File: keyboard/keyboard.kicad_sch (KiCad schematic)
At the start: 19 parts, among them U1 Raspberry_Pi_Pico

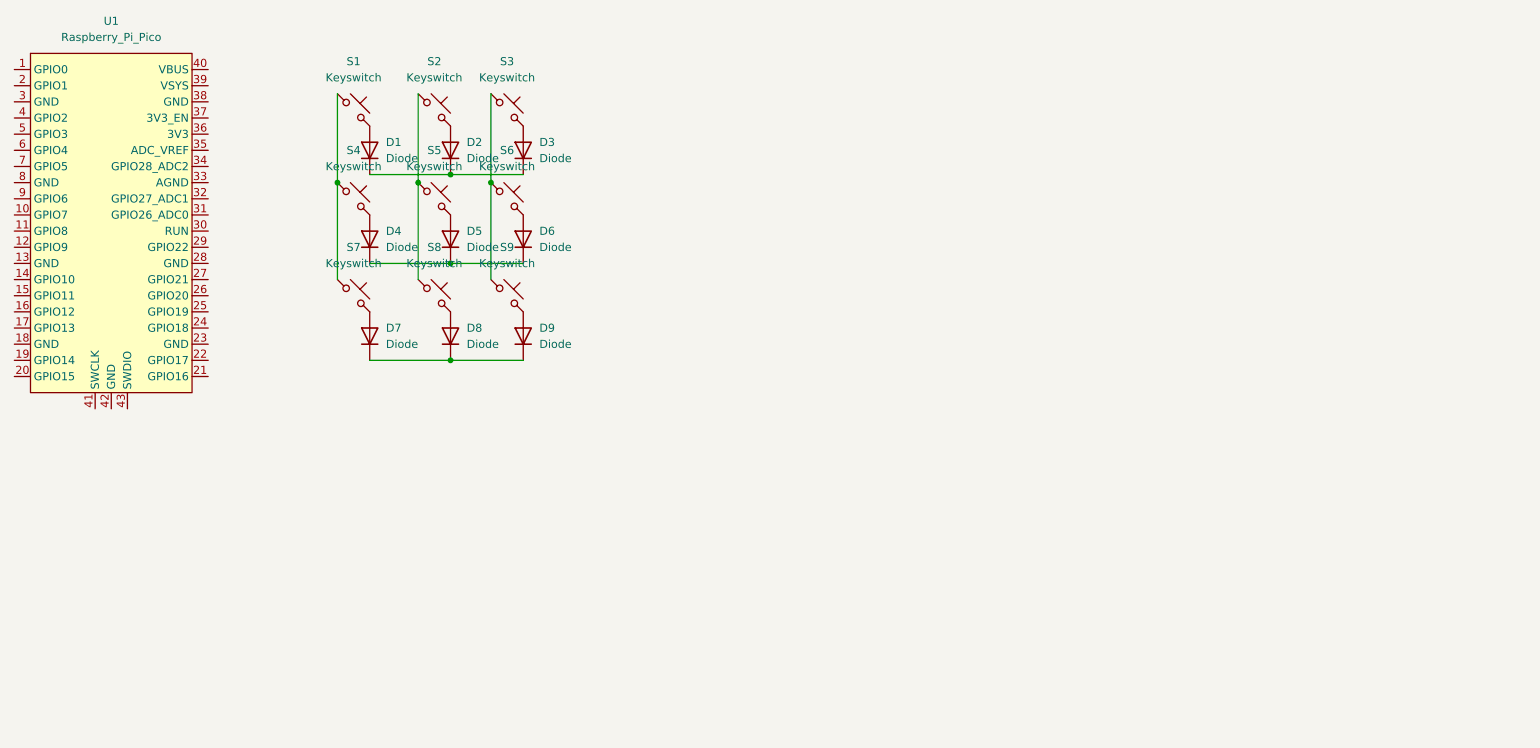
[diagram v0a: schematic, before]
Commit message: schema 5x12 keys
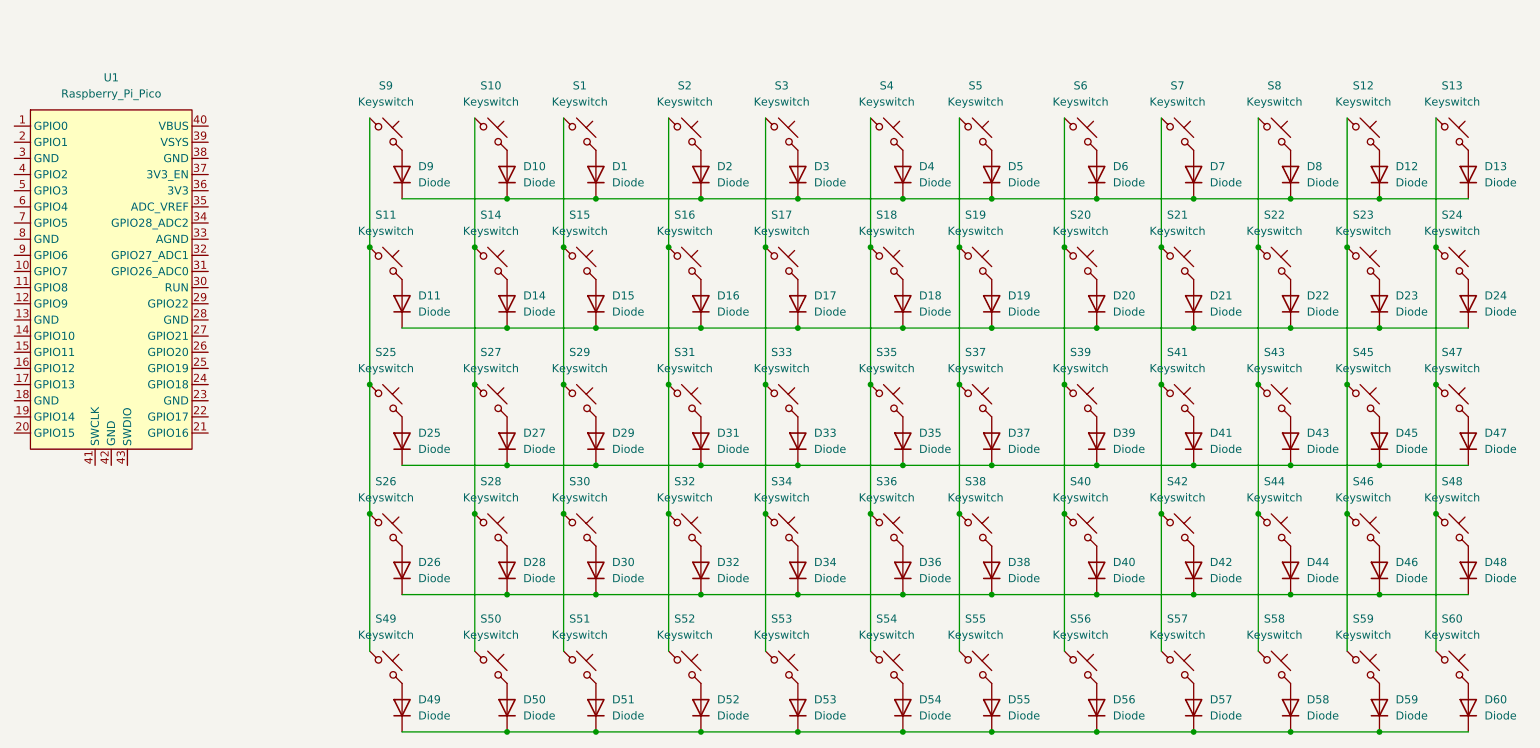
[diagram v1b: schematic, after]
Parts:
- added D10, D11, D12, D13, D14, D15, D16, D17, D18, D19, D20, D21, D22, D23, D24, D25, D26, D27, D28, D29, D30, D31, D32, D33, D34, D35, D36, D37, D38, D39, D40, D41, D42, D43, D44, D45, D46, D47, D48, D49, D50, D51, D52, D53, D54, D55, D56, D57, D58, D59, D60: Diode, symbol ScottoKeebs:Placeholder_Diode
- added S10, S11, S12, S13, S14, S15, S16, S17, S18, S19, S20, S21, S22, S23, S24, S25, S26, S27, S28, S29, S30, S31, S32, S33, S34, S35, S36, S37, S38, S39, S40, S41, S42, S43, S44, S45, S46, S47, S48, S49, S50, S51, S52, S53, S54, S55, S56, S57, S58, S59, S60: Keyswitch, symbol ScottoKeebs:Placeholder_Keyswitch
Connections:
- net at D1.1 (K), D2.1 (K), D3.1 (K): now also D4.1 (K), D5.1 (K), D6.1 (K), D7.1 (K), D8.1 (K), D9.1 (K), D10.1 (K), D12.1 (K), D13.1 (K)
- new net: S20.1, S39.1, S40.1, S56.1, S6.1
- new net: D20.2 (A), S20.2
- new net: D10.2 (A), S10.2
- new net: S10.1, S14.1, S27.1, S28.1, S50.1
- new net: D56.2 (A), S56.2
- new net: S18.1, S35.1, S36.1, S4.1, S54.1
- new net: D54.2 (A), S54.2
- new net: D25.1 (K), D27.1 (K), D29.1 (K), D31.1 (K), D33.1 (K), D35.1 (K), D37.1 (K), D39.1 (K), D41.1 (K), D43.1 (K), D45.1 (K), D47.1 (K)
- new net: D35.2 (A), S35.2
- new net: D11.1 (K), D14.1 (K), D15.1 (K), D16.1 (K), D17.1 (K), D18.1 (K), D19.1 (K), D20.1 (K), D21.1 (K), D22.1 (K), D23.1 (K), D24.1 (K)
- new net: D13.2 (A), S13.2
- new net: D40.2 (A), S40.2
- new net: S16.1, S2.1, S31.1, S32.1, S52.1
- new net: D49.1 (K), D50.1 (K), D51.1 (K), D52.1 (K), D53.1 (K), D54.1 (K), D55.1 (K), D56.1 (K), D57.1 (K), D58.1 (K), D59.1 (K), D60.1 (K)
- new net: D53.2 (A), S53.2
- new net: S19.1, S37.1, S38.1, S5.1, S55.1
- new net: D50.2 (A), S50.2
- new net: D26.1 (K), D28.1 (K), D30.1 (K), D32.1 (K), D34.1 (K), D36.1 (K), D38.1 (K), D40.1 (K), D42.1 (K), D44.1 (K), D46.1 (K), D48.1 (K)
- new net: D30.2 (A), S30.2
- new net: D18.2 (A), S18.2
- new net: S22.1, S43.1, S44.1, S58.1, S8.1
- new net: D58.2 (A), S58.2
- new net: D29.2 (A), S29.2
- new net: D42.2 (A), S42.2
- new net: D36.2 (A), S36.2
- new net: D55.2 (A), S55.2
- new net: D16.2 (A), S16.2
- new net: D28.2 (A), S28.2
- new net: S11.1, S25.1, S26.1, S49.1, S9.1
- new net: D11.2 (A), S11.2
- new net: S13.1, S24.1, S47.1, S48.1, S60.1
- new net: D47.2 (A), S47.2
- new net: S1.1, S15.1, S29.1, S30.1, S51.1
- new net: D51.2 (A), S51.2
- new net: D59.2 (A), S59.2
- new net: D24.2 (A), S24.2
- new net: D43.2 (A), S43.2
- new net: D48.2 (A), S48.2
- new net: D57.2 (A), S57.2
- new net: D26.2 (A), S26.2
- new net: D32.2 (A), S32.2
- new net: S12.1, S23.1, S45.1, S46.1, S59.1
- new net: D45.2 (A), S45.2
- new net: S21.1, S41.1, S42.1, S57.1, S7.1
- new net: S17.1, S3.1, S33.1, S34.1, S53.1
- new net: D34.2 (A), S34.2
- new net: D38.2 (A), S38.2
- new net: D49.2 (A), S49.2
- new net: D33.2 (A), S33.2
- new net: D46.2 (A), S46.2
- new net: D39.2 (A), S39.2
- new net: D12.2 (A), S12.2
- new net: D21.2 (A), S21.2
- new net: D52.2 (A), S52.2
- new net: D17.2 (A), S17.2
- new net: D44.2 (A), S44.2
- new net: D15.2 (A), S15.2
- new net: D37.2 (A), S37.2
- new net: D22.2 (A), S22.2
- new net: D14.2 (A), S14.2
- new net: D27.2 (A), S27.2
- new net: D31.2 (A), S31.2
- new net: D19.2 (A), S19.2
- new net: D25.2 (A), S25.2
- new net: D23.2 (A), S23.2
- new net: D41.2 (A), S41.2
- new net: D60.2 (A), S60.2
